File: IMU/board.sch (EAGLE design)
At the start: 10 parts

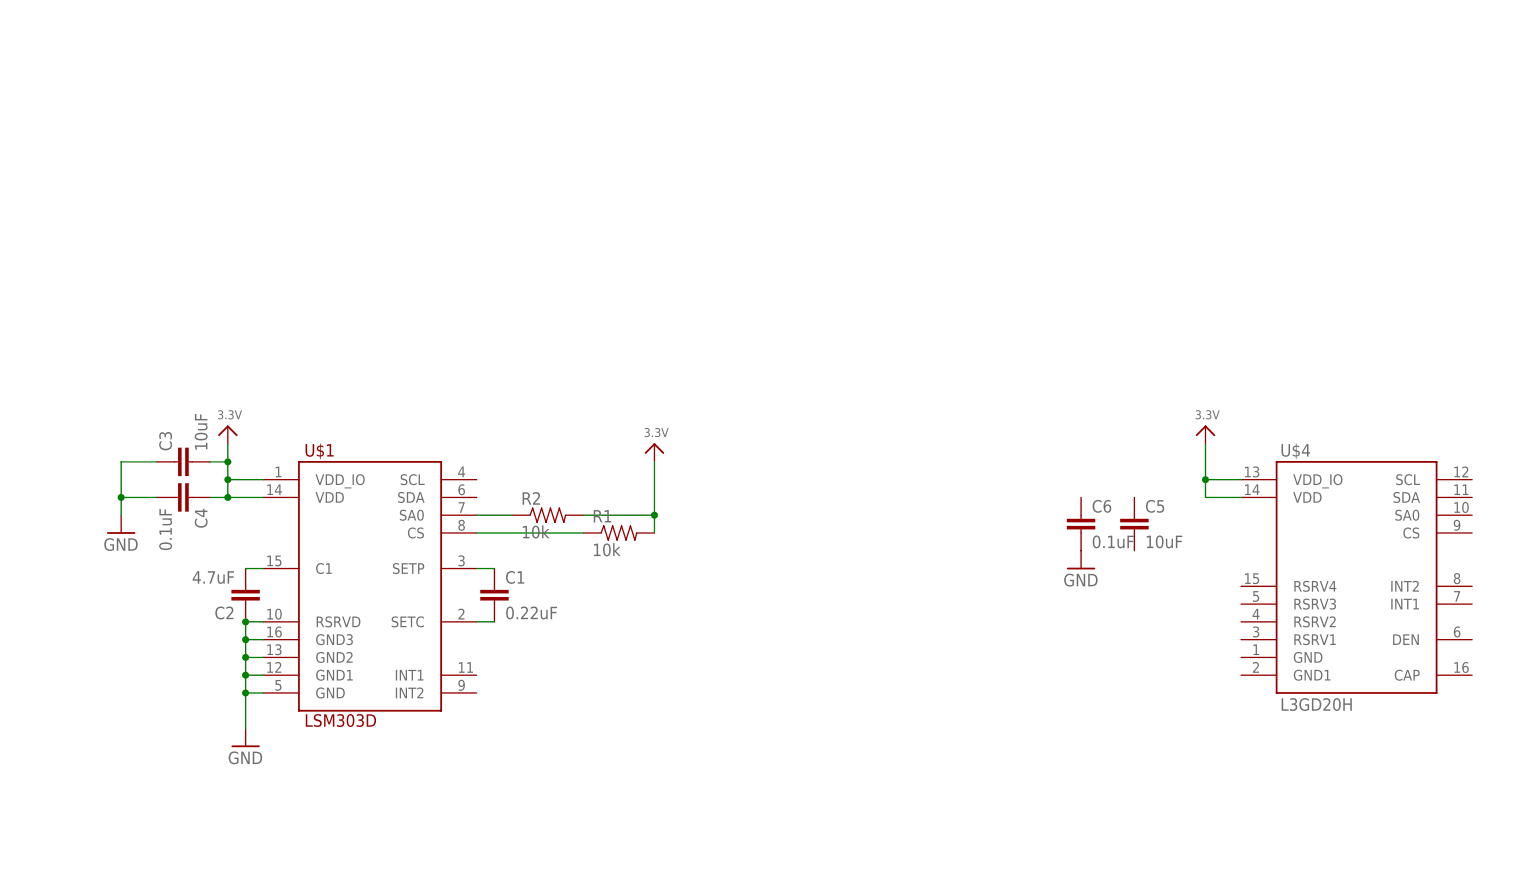
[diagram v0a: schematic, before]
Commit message: Finished gyro portion of schematic
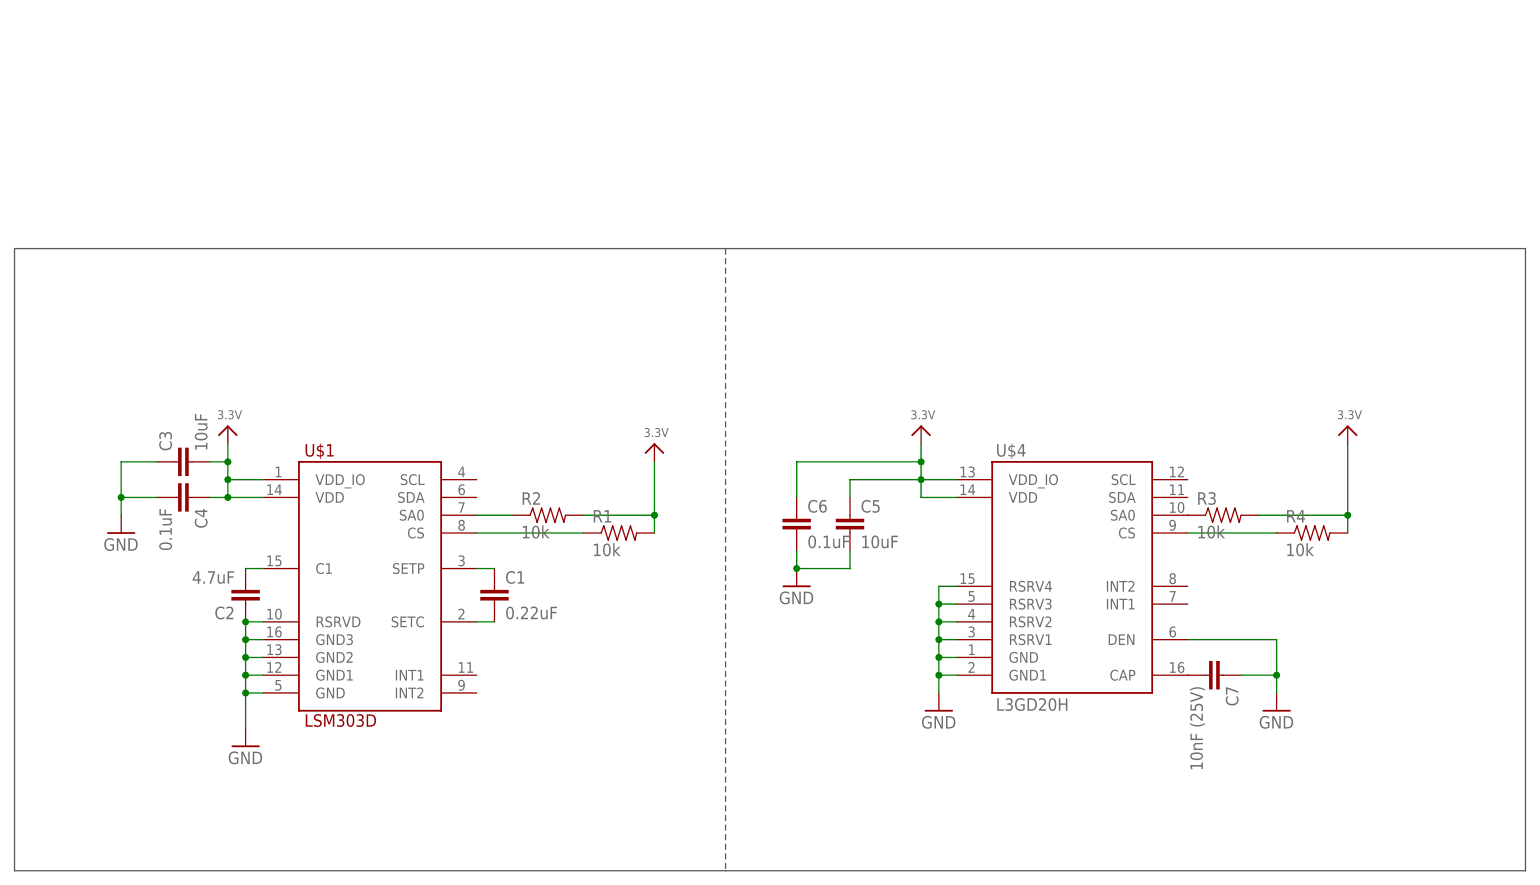
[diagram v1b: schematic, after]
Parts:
- added C7: 10nF (25V), SparkFun-Capacitors:CAP0805
- added R3, R4: 10k, SparkFun-Passives:RESISTOR0805-RES
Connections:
- new net N$6: R3.1, U$4.SA0
- new net N$7: R4.1, U$4.CS
- new net N$8: C7.2, U$4.CAP
- net 3.3V: now also C5.1, C6.1, R3.2, R4.2
- net GND: now also C5.2, C7.1, U$4.DEN, U$4.GND, U$4.GND1, U$4.RSRV1, U$4.RSRV2, U$4.RSRV3, U$4.RSRV4
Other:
- moved on the sheet: C5, C6, U$4
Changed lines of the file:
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@@
 <part name="C5" library="SparkFun-Capacitors" deviceset="CAP" device="0805" value="10uF"/>
 <part name="C6" library="SparkFun-Capacitors" deviceset="CAP" device="0805" value="0.1uF"/>
+<part name="GND4" library="SparkFun-Aesthetics" deviceset="GND" device=""/>
+<part name="U$6" library="microbuilder" deviceset="3.3V" device=""/>
+<part name="R3" library="SparkFun-Passives" deviceset="RESISTOR" device="0805-RES" value="10k"/>
+<part name="R4" library="SparkFun-Passives" deviceset="RESISTOR" device="0805-RES" value="10k"/>
+<part name="C7" library="SparkFun-Capacitors" deviceset="CAP" device="0805" value="10nF (25V)"/>
+<part name="GND5" library="SparkFun-Aesthetics" deviceset="GND" device=""/>
 </parts>
 <sheets>
 <sheet>
 <plain>
+<wire x1="-15.24" y1="-2.54" x2="86.36" y2="-2.54" width="0.1524" layer="97"/>
+<wire x1="86.36" y1="-2.54" x2="200.66" y2="-2.54" width="0.1524" layer="97"/>
+<wire x1="200.66" y1="-2.54" x2="200.66" y2="86.36" width="0.1524" layer="97"/>
+<wire x1="200.66" y1="86.36" x2="86.36" y2="86.36" width="0.1524" layer="97"/>
+<wire x1="86.36" y1="86.36" x2="-15.24" y2="86.36" width="0.1524" layer="97"/>
+<wire x1="-15.24" y1="86.36" x2="-15.24" y2="-2.54" width="0.1524" layer="97"/>
+<wire x1="86.36" y1="86.36" x2="86.36" y2="-2.54" width="0.1524" layer="97" style="shortdash"/>
 </plain>
 <instances>
@@
 <instance part="C3" gate="G$1" x="10.16" y="55.88" rot="R90"/>
 <instance part="C4" gate="G$1" x="7.62" y="50.8" rot="R270"/>
-<instance part="U$4" gate="G$1" x="172.72" y="35.56"/>
-<instance part="U$5" gate="G$1" x="154.94" y="60.96"/>
-<instance part="GND3" gate="1" x="137.16" y="40.64"/>
-<instance part="C5" gate="G$1" x="144.78" y="45.72"/>
-<instance part="C6" gate="G$1" x="137.16" y="45.72"/>
+<instance part="U$4" gate="G$1" x="132.08" y="35.56"/>
+<instance part="U$5" gate="G$1" x="114.3" y="60.96"/>
+<instance part="GND3" gate="1" x="96.52" y="38.1"/>
+<instance part="C5" gate="G$1" x="104.14" y="45.72"/>
+<instance part="C6" gate="G$1" x="96.52" y="45.72"/>
+<instance part="GND4" gate="1" x="116.84" y="20.32"/>
+<instance part="U$6" gate="G$1" x="175.26" y="60.96"/>
+<instance part="R3" gate="G$1" x="157.48" y="48.26"/>
+<instance part="R4" gate="G$1" x="170.18" y="45.72"/>
+<instance part="C7" gate="G$1" x="154.94" y="25.4" rot="R270"/>
+<instance part="GND5" gate="1" x="165.1" y="20.32"/>
 </instances>
 <busses>
@@
 <segment>
 <pinref part="U$4" gate="G$1" pin="VDD_IO"/>
-<wire x1="160.02" y1="53.34" x2="154.94" y2="53.34" width="0.1524" layer="91"/>
+<wire x1="119.38" y1="53.34" x2="114.3" y2="53.34" width="0.1524" layer="91"/>
 <pinref part="U$5" gate="G$1" pin="3.3V"/>
-<wire x1="154.94" y1="53.34" x2="154.94" y2="58.42" width="0.1524" layer="91"/>
+<wire x1="114.3" y1="53.34" x2="114.3" y2="55.88" width="0.1524" layer="91"/>
 <pinref part="U$4" gate="G$1" pin="VDD"/>
-<wire x1="160.02" y1="50.8" x2="154.94" y2="50.8" width="0.1524" layer="91"/>
-<wire x1="154.94" y1="50.8" x2="154.94" y2="53.34" width="0.1524" layer="91"/>
-<junction x="154.94" y="53.34"/>
+<wire x1="114.3" y1="55.88" x2="114.3" y2="58.42" width="0.1524" layer="91"/>
+<wire x1="119.38" y1="50.8" x2="114.3" y2="50.8" width="0.1524" layer="91"/>
+<wire x1="114.3" y1="50.8" x2="114.3" y2="53.34" width="0.1524" layer="91"/>
+<junction x="114.3" y="53.34"/>
+<pinref part="C6" gate="G$1" pin="1"/>
+<wire x1="96.52" y1="50.8" x2="96.52" y2="55.88" width="0.1524" layer="91"/>
+<wire x1="96.52" y1="55.88" x2="114.3" y2="55.88" width="0.1524" layer="91"/>
+<junction x="114.3" y="55.88"/>
+<pinref part="C5" gate="G$1" pin="1"/>
+<wire x1="104.14" y1="50.8" x2="104.14" y2="53.34" width="0.1524" layer="91"/>
+<wire x1="104.14" y1="53.34" x2="114.3" y2="53.34" width="0.1524" layer="91"/>
+</segment>
+<segment>
+<pinref part="R4" gate="G$1" pin="2"/>
+<pinref part="U$6" gate="G$1" pin="3.3V"/>
+<wire x1="175.26" y1="45.72" x2="175.26" y2="48.26" width="0.1524" layer="91"/>
+<pinref part="R3" gate="G$1" pin="2"/>
+<wire x1="175.26" y1="48.26" x2="175.26" y2="58.42" width="0.1524" layer="91"/>
+<wire x1="162.56" y1="48.26" x2="175.26" y2="48.26" width="0.1524" layer="91"/>
+<junction x="175.26" y="48.26"/>
 </segment>
 </net>
@@
 <pinref part="GND3" gate="1" pin="GND"/>
 <pinref part="C6" gate="G$1" pin="2"/>
+<wire x1="96.52" y1="40.64" x2="96.52" y2="43.18" width="0.1524" layer="91"/>
+<pinref part="C5" gate="G$1" pin="2"/>
+<wire x1="104.14" y1="43.18" x2="104.14" y2="40.64" width="0.1524" layer="91"/>
+<wire x1="104.14" y1="40.64" x2="96.52" y2="40.64" width="0.1524" layer="91"/>
+<junction x="96.52" y="40.64"/>
+</segment>
+<segment>
+<pinref part="U$4" gate="G$1" pin="RSRV4"/>
+<pinref part="GND4" gate="1" pin="GND"/>
+<wire x1="119.38" y1="38.1" x2="116.84" y2="38.1" width="0.1524" layer="91"/>
+<wire x1="116.84" y1="38.1" x2="116.84" y2="35.56" width="0.1524" layer="91"/>
+<pinref part="U$4" gate="G$1" pin="RSRV3"/>
+<wire x1="116.84" y1="35.56" x2="116.84" y2="33.02" width="0.1524" layer="91"/>
+<wire x1="116.84" y1="33.02" x2="116.84" y2="30.48" width="0.1524" layer="91"/>
+<wire x1="116.84" y1="30.48" x2="116.84" y2="27.94" width="0.1524" layer="91"/>
+<wire x1="116.84" y1="27.94" x2="116.84" y2="25.4" width="0.1524" layer="91"/>
+<wire x1="116.84" y1="25.4" x2="116.84" y2="22.86" width="0.1524" layer="91"/>
+<wire x1="119.38" y1="35.56" x2="116.84" y2="35.56" width="0.1524" layer="91"/>
+<junction x="116.84" y="35.56"/>
+<pinref part="U$4" gate="G$1" pin="RSRV2"/>
+<wire x1="119.38" y1="33.02" x2="116.84" y2="33.02" width="0.1524" layer="91"/>
+<junction x="116.84" y="33.02"/>
+<pinref part="U$4" gate="G$1" pin="RSRV1"/>
+<wire x1="119.38" y1="30.48" x2="116.84" y2="30.48" width="0.1524" layer="91"/>
+<junction x="116.84" y="30.48"/>
+<pinref part="U$4" gate="G$1" pin="GND"/>
+<wire x1="119.38" y1="27.94" x2="116.84" y2="27.94" width="0.1524" layer="91"/>
+<junction x="116.84" y="27.94"/>
+<pinref part="U$4" gate="G$1" pin="GND1"/>
+<wire x1="119.38" y1="25.4" x2="116.84" y2="25.4" width="0.1524" layer="91"/>
+<junction x="116.84" y="25.4"/>
+</segment>
+<segment>
+<pinref part="U$4" gate="G$1" pin="DEN"/>
+<wire x1="152.4" y1="30.48" x2="165.1" y2="30.48" width="0.1524" layer="91"/>
+<pinref part="GND5" gate="1" pin="GND"/>
+<wire x1="165.1" y1="30.48" x2="165.1" y2="25.4" width="0.1524" layer="91"/>
+<pinref part="C7" gate="G$1" pin="1"/>
+<wire x1="165.1" y1="25.4" x2="165.1" y2="22.86" width="0.1524" layer="91"/>
+<wire x1="160.02" y1="25.4" x2="165.1" y2="25.4" width="0.1524" layer="91"/>
+<junction x="165.1" y="25.4"/>
 </segment>
 </net>
@@
 </segment>
 </net>
+<net name="N$6" class="0">
+<segment>
+<pinref part="U$4" gate="G$1" pin="SA0"/>
+<pinref part="R3" gate="G$1" pin="1"/>
+</segment>
+</net>
+<net name="N$7" class="0">
+<segment>
+<pinref part="U$4" gate="G$1" pin="CS"/>
+<pinref part="R4" gate="G$1" pin="1"/>
+<wire x1="152.4" y1="45.72" x2="165.1" y2="45.72" width="0.1524" layer="91"/>
+</segment>
+</net>
+<net name="N$8" class="0">
+<segment>
+<pinref part="U$4" gate="G$1" pin="CAP"/>
+<pinref part="C7" gate="G$1" pin="2"/>
+</segment>
+</net>

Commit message: Reviewer tags in library
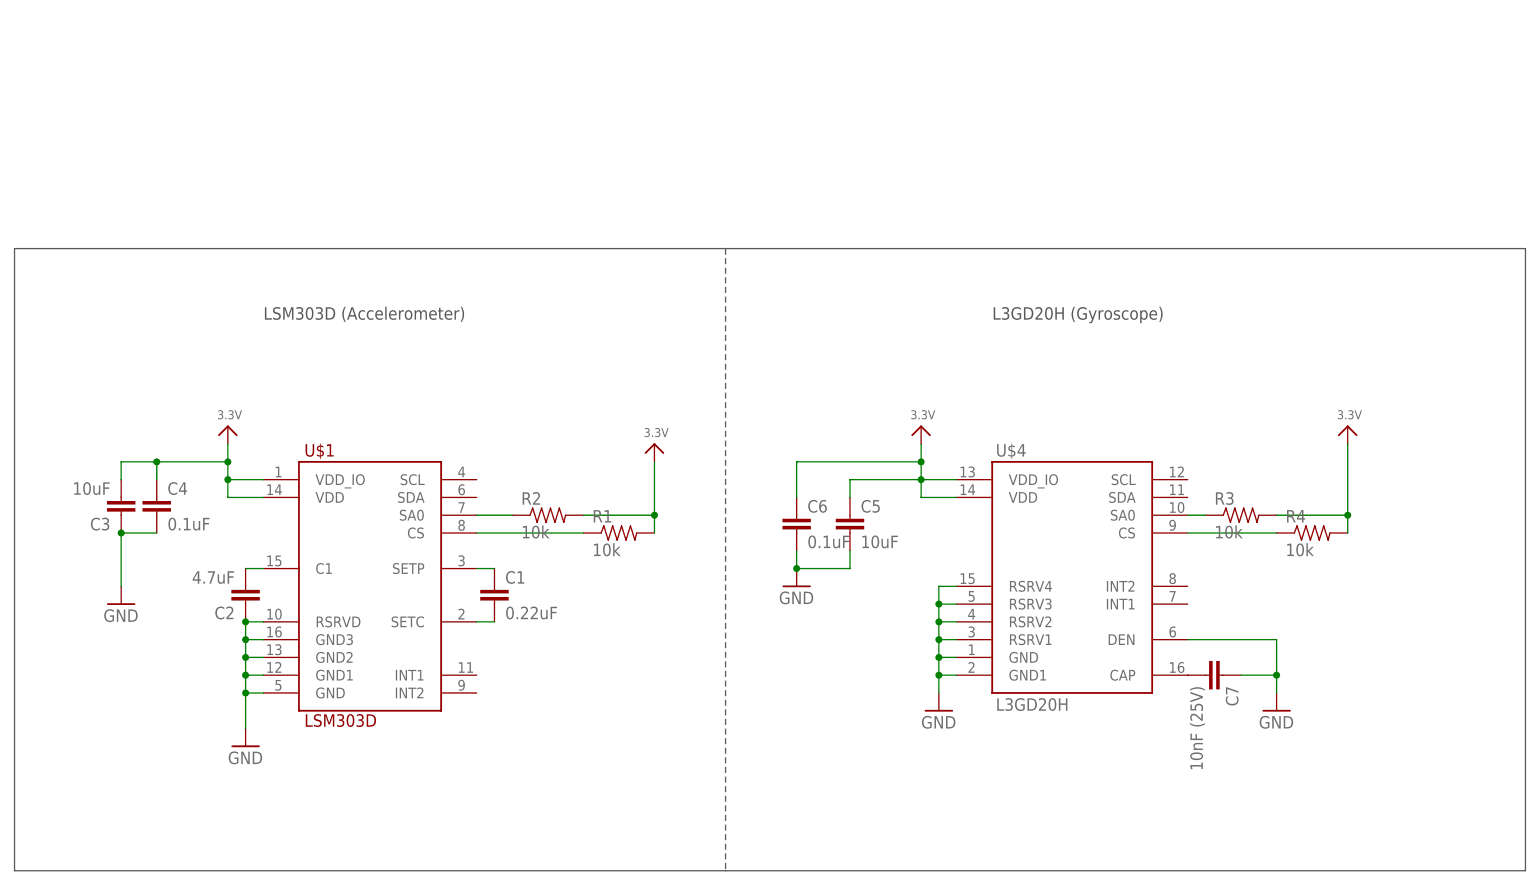
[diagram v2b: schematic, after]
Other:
- note added: "L3GD20H (Gyroscope)"
- note added: "LSM303D (Accelerometer)"
- moved on the sheet: C3, C4, R3
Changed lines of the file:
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@@
 <setting verticaltext="up"/>
 </settings>
-<grid distance="0.1" unitdist="inch" unit="inch" style="lines" multiple="1" display="yes" altdistance="0.01" altunitdist="inch" altunit="inch"/>
+<grid distance="0.1" unitdist="inch" unit="inch" style="lines" multiple="1" display="no" altdistance="0.01" altunitdist="inch" altunit="inch"/>
 <layers>
 <layer number="1" name="Top" color="4" fill="1" visible="no" active="no"/>
@@
 <wire x1="-15.24" y1="86.36" x2="-15.24" y2="-2.54" width="0.1524" layer="97"/>
 <wire x1="86.36" y1="86.36" x2="86.36" y2="-2.54" width="0.1524" layer="97" style="shortdash"/>
+<text x="20.32" y="76.2" size="1.778" layer="97">LSM303D (Accelerometer)</text>
+<text x="124.46" y="76.2" size="1.778" layer="97">L3GD20H (Gyroscope)</text>
 </plain>
 <instances>
@@
 <instance part="U$3" gate="G$1" x="15.24" y="60.96"/>
 <instance part="C2" gate="G$1" x="17.78" y="38.1" rot="R180"/>
-<instance part="GND1" gate="1" x="0" y="45.72"/>
-<instance part="C3" gate="G$1" x="10.16" y="55.88" rot="R90"/>
-<instance part="C4" gate="G$1" x="7.62" y="50.8" rot="R270"/>
+<instance part="GND1" gate="1" x="0" y="35.56"/>
+<instance part="C3" gate="G$1" x="0" y="50.8" rot="R180"/>
+<instance part="C4" gate="G$1" x="5.08" y="48.26"/>
 <instance part="U$4" gate="G$1" x="132.08" y="35.56"/>
 <instance part="U$5" gate="G$1" x="114.3" y="60.96"/>
@@
 <instance part="GND4" gate="1" x="116.84" y="20.32"/>
 <instance part="U$6" gate="G$1" x="175.26" y="60.96"/>
-<instance part="R3" gate="G$1" x="157.48" y="48.26"/>
+<instance part="R3" gate="G$1" x="160.02" y="48.26"/>
 <instance part="R4" gate="G$1" x="170.18" y="45.72"/>
 <instance part="C7" gate="G$1" x="154.94" y="25.4" rot="R270"/>
@@
 <segment>
 <pinref part="U$3" gate="G$1" pin="3.3V"/>
+<pinref part="U$1" gate="G$1" pin="VDD_IO"/>
 <wire x1="15.24" y1="58.42" x2="15.24" y2="55.88" width="0.1524" layer="91"/>
-<pinref part="U$1" gate="G$1" pin="VDD_IO"/>
 <wire x1="15.24" y1="55.88" x2="15.24" y2="53.34" width="0.1524" layer="91"/>
 <wire x1="15.24" y1="53.34" x2="20.32" y2="53.34" width="0.1524" layer="91"/>
@@
 <wire x1="15.24" y1="50.8" x2="15.24" y2="53.34" width="0.1524" layer="91"/>
 <junction x="15.24" y="53.34"/>
+<pinref part="C3" gate="G$1" pin="2"/>
+<wire x1="0" y1="53.34" x2="0" y2="55.88" width="0.1524" layer="91"/>
+<wire x1="0" y1="55.88" x2="5.08" y2="55.88" width="0.1524" layer="91"/>
+<junction x="15.24" y="55.88"/>
 <pinref part="C4" gate="G$1" pin="1"/>
-<wire x1="15.24" y1="50.8" x2="12.7" y2="50.8" width="0.1524" layer="91"/>
-<junction x="15.24" y="50.8"/>
-<pinref part="C3" gate="G$1" pin="2"/>
-<wire x1="15.24" y1="55.88" x2="12.7" y2="55.88" width="0.1524" layer="91"/>
-<junction x="15.24" y="55.88"/>
+<wire x1="5.08" y1="55.88" x2="15.24" y2="55.88" width="0.1524" layer="91"/>
+<wire x1="5.08" y1="53.34" x2="5.08" y2="55.88" width="0.1524" layer="91"/>
+<junction x="5.08" y="55.88"/>
 </segment>
 <segment>
@@
 <pinref part="R3" gate="G$1" pin="2"/>
 <wire x1="175.26" y1="48.26" x2="175.26" y2="58.42" width="0.1524" layer="91"/>
-<wire x1="162.56" y1="48.26" x2="175.26" y2="48.26" width="0.1524" layer="91"/>
+<wire x1="165.1" y1="48.26" x2="175.26" y2="48.26" width="0.1524" layer="91"/>
 <junction x="175.26" y="48.26"/>
 </segment>
@@
 <pinref part="C2" gate="G$1" pin="1"/>
 <junction x="17.78" y="33.02"/>
-</segment>
-<segment>
-<pinref part="C3" gate="G$1" pin="1"/>
-<wire x1="5.08" y1="55.88" x2="0" y2="55.88" width="0.1524" layer="91"/>
-<pinref part="GND1" gate="1" pin="GND"/>
-<wire x1="0" y1="55.88" x2="0" y2="50.8" width="0.1524" layer="91"/>
-<pinref part="C4" gate="G$1" pin="2"/>
-<wire x1="0" y1="50.8" x2="0" y2="48.26" width="0.1524" layer="91"/>
-<wire x1="5.08" y1="50.8" x2="0" y2="50.8" width="0.1524" layer="91"/>
-<junction x="0" y="50.8"/>
 </segment>
 <segment>
@@
 <junction x="165.1" y="25.4"/>
 </segment>
+<segment>
+<pinref part="C4" gate="G$1" pin="2"/>
+<pinref part="C3" gate="G$1" pin="1"/>
+<wire x1="5.08" y1="45.72" x2="0" y2="45.72" width="0.1524" layer="91"/>
+<pinref part="GND1" gate="1" pin="GND"/>
+<wire x1="0" y1="45.72" x2="0" y2="38.1" width="0.1524" layer="91"/>
+<junction x="0" y="45.72"/>
+</segment>
 </net>
 <net name="N$5" class="0">
@@
 <pinref part="U$4" gate="G$1" pin="SA0"/>
 <pinref part="R3" gate="G$1" pin="1"/>
-</segment>
-</net>
+<wire x1="154.94" y1="48.26" x2="152.4" y2="48.26" width="0.1524" layer="91"/>
+</segment>
+</net>
